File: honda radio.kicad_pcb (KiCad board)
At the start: 2 copper layers, 124.5 x 123 mm, 81 parts, among them J1 DE9_Receptacle_MountingHoles, J2 DE9_Receptacle_MountingHoles, J3 DB25_Receptacle_MountingHoles, J4 RCA Jack, J5 SJ-3523-SMT-TR, J6 Arduino Nano Every, J7 Adafruit MPM3610, J8 TinySine AudioB Plus V3r2, K1 G6L-1F-TR_DC5, K10 G6L-1F-TR_DC5, K11 G6L-1F-TR_DC5, K12 G6L-1F-TR_DC5, K2 G6L-1F-TR_DC5, K3 G6L-1F-TR_DC5, K4 G6L-1F-TR_DC5, K5 G6L-1F-TR_DC5, K6 G6L-1F-TR_DC5, K7 G6L-1F-TR_DC5, K8 G6L-1F-TR_DC5, K9 G2RL-2A-DC5, Q1 BC547, Q10 BC547, Q11 BC547, Q12 BC547, Q2 BC547, Q3 BC547, Q4 BC547, Q5 BC547, Q6 BC547, Q7 BC547, Q8 BC547, Q9 BC547

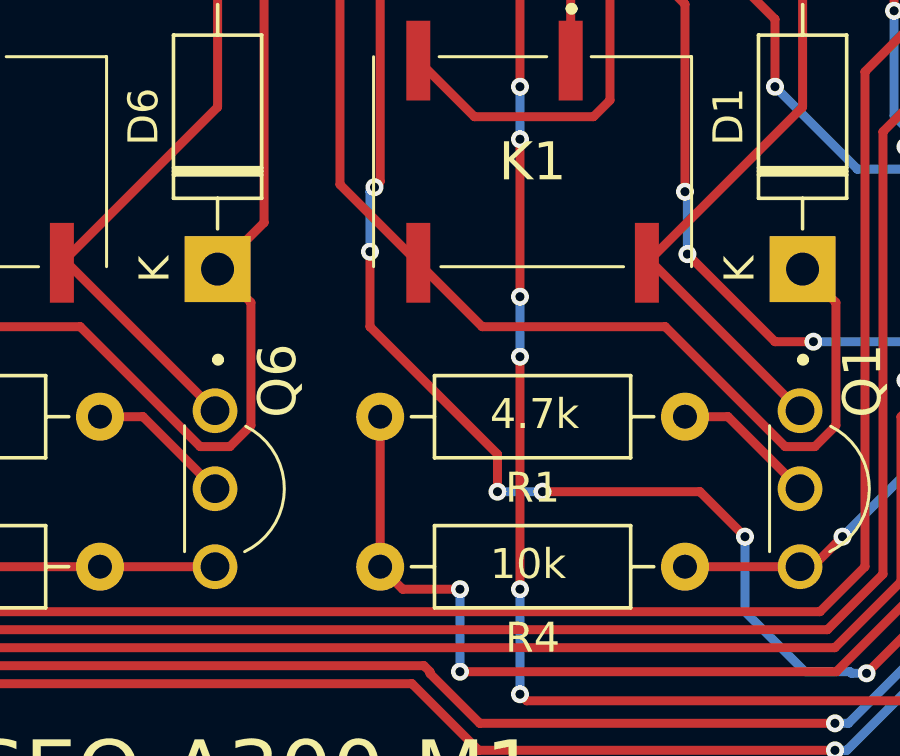
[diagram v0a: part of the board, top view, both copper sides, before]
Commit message: added missing trace
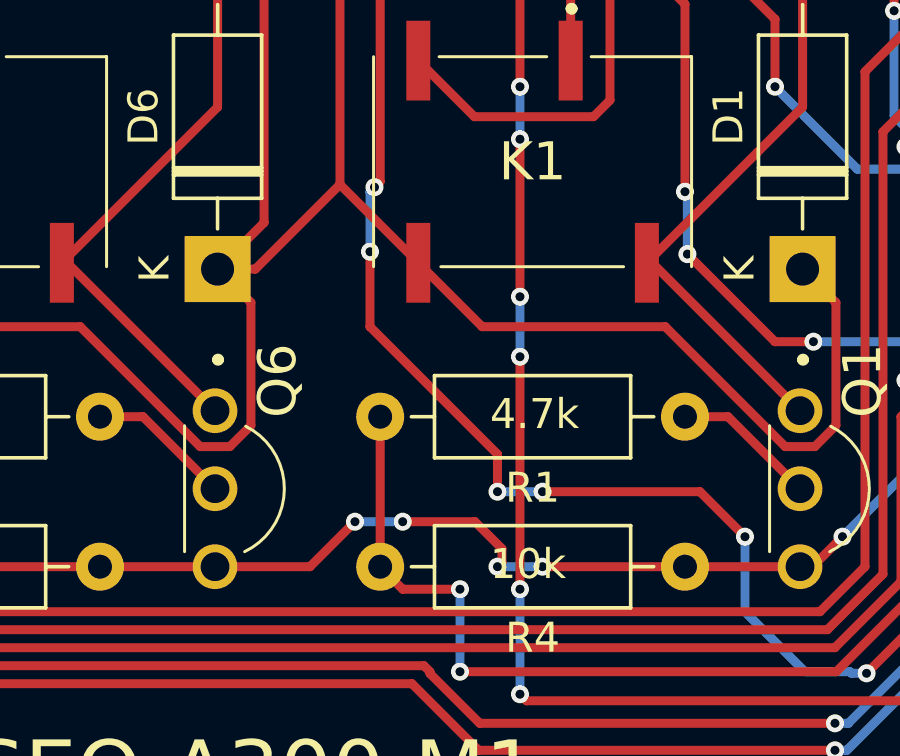
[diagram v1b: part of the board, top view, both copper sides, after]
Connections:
- D10 pad 1: Net-(D10-K) -> Net-(D1-K)
- D11 pad 1: Net-(D10-K) -> Net-(D1-K)
- D12 pad 1: Net-(D10-K) -> Net-(D1-K)
- D6 pad 1: Net-(D10-K) -> Net-(D1-K)
- D7 pad 1: Net-(D10-K) -> Net-(D1-K)
- D8 pad 1: Net-(D10-K) -> Net-(D1-K)
- K10 pad 5: Net-(D10-K) -> Net-(D1-K)
- K11 pad 5: Net-(D10-K) -> Net-(D1-K)
- K12 pad 5: Net-(D10-K) -> Net-(D1-K)
- K6 pad 5: Net-(D10-K) -> Net-(D1-K)
- K7 pad 5: Net-(D10-K) -> Net-(D1-K)
- K8 pad 5: Net-(D10-K) -> Net-(D1-K)
- Q10 pad 3: Net-(Q10-E) -> Net-(J1-GND)
- Q11 pad 3: Net-(Q10-E) -> Net-(J1-GND)
- Q12 pad 3: Net-(Q10-E) -> Net-(J1-GND)
- Q6 pad 3: Net-(Q10-E) -> Net-(J1-GND)
- Q7 pad 3: Net-(Q10-E) -> Net-(J1-GND)
- Q8 pad 3: Net-(Q10-E) -> Net-(J1-GND)
- R20 pad 1: Net-(Q10-E) -> Net-(J1-GND)
- R21 pad 1: Net-(Q10-E) -> Net-(J1-GND)
- R22 pad 1: Net-(Q10-E) -> Net-(J1-GND)
- R31 pad 1: Net-(Q10-E) -> Net-(J1-GND)
- R32 pad 1: Net-(Q10-E) -> Net-(J1-GND)
- R33 pad 1: Net-(Q10-E) -> Net-(J1-GND)
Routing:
- net Net-(D1-K): track 335.9 -> 547.6 mm
- net Net-(D10-K): track 206.5 -> 0.00 mm
- net Net-(J1-GND): track 484.1 -> 627.0 mm, vias 10 -> 26
- net Net-(Q10-E): track 125.4 -> 0.00 mm, vias 12 -> 0
